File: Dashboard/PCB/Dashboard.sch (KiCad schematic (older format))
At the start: 91 parts, among them J1 Display, J2 Conn_01x26_Female, J3 LED, J7 PROGRAMMER, SW1 SW_SPST, U1 STM32F767ZIT6, U10 24LC01, U3 MP2359DJ-LF-Z, U4 AS4C1M16S-6TCN, U5 AT25SF128A-SHB-T, U6 MP2332H, U7 MCP2561-E-SN, U8 MCP2561-E-SN, U9 ESP-12S, Y1 Crystal_GND24

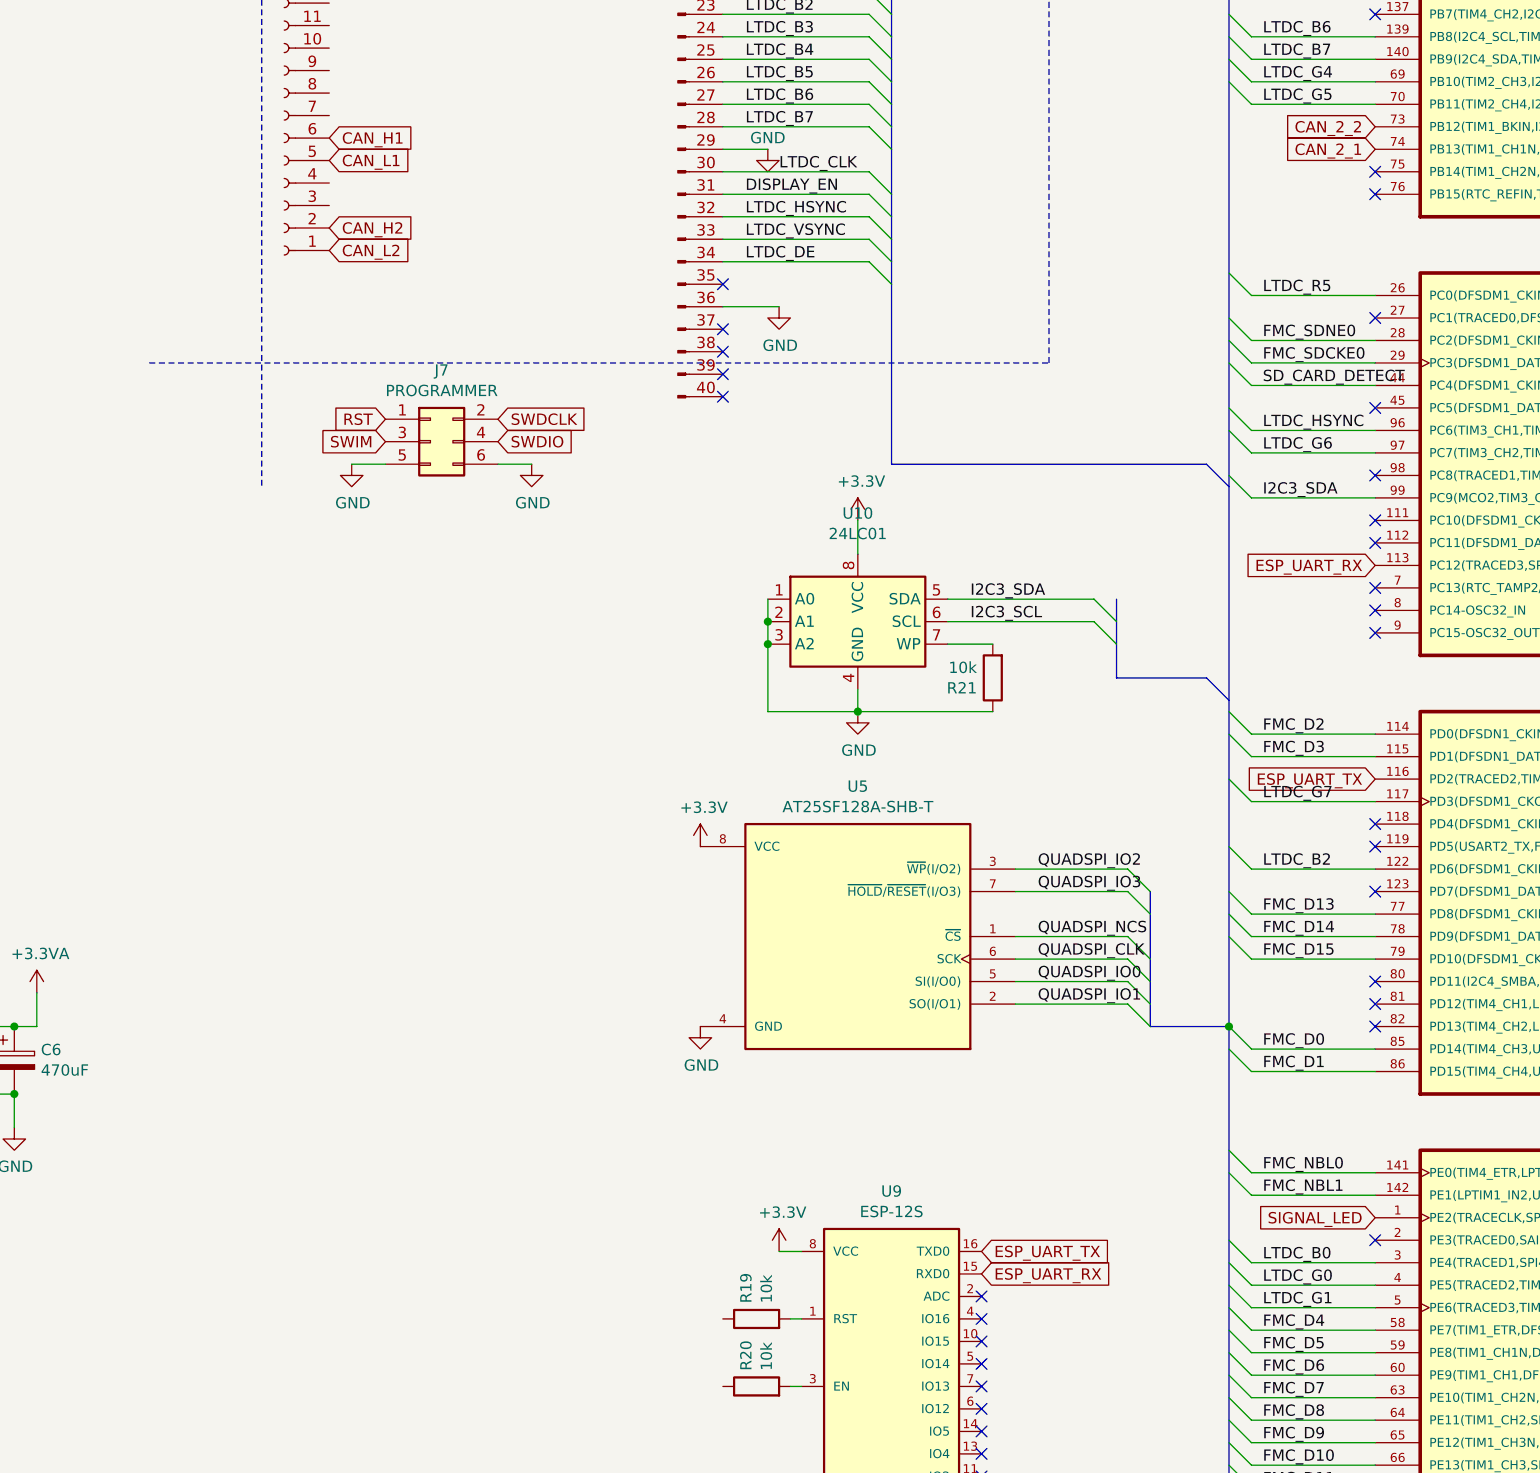
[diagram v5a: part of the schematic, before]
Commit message: Add usb C to board
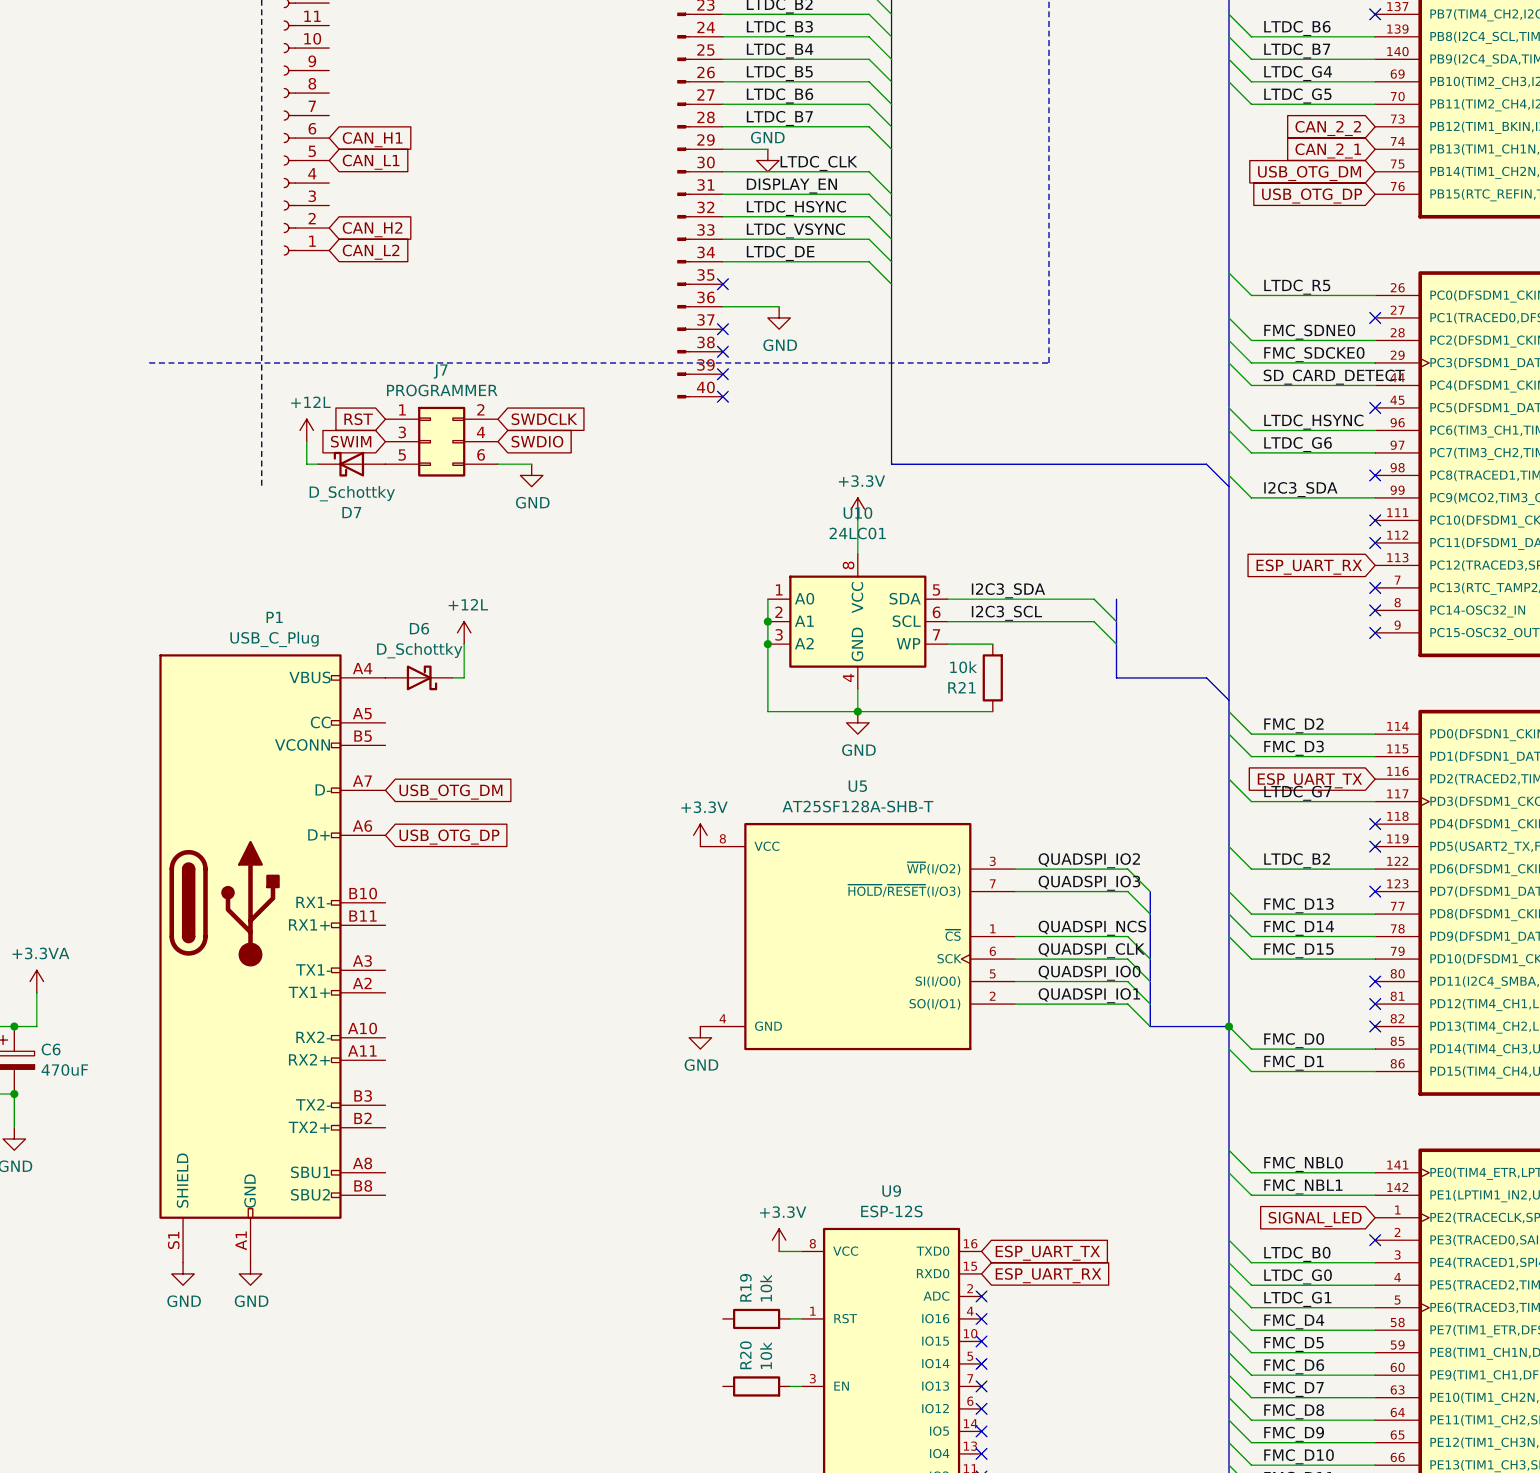
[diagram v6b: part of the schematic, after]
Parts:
- added D6, D7: D_Schottky, Diode_SMD:D_0805_2012Metric_Pad1.15x1.40mm_HandSolder, symbol Device:D_Schottky
- added P1: USB_C_Plug, Connector_USB:USB_C_Receptacle_Amphenol_12401548E4-2A, symbol Connector:USB_C_Plug
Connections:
- net +12L: now also D6.1 (K), D7.1 (K)
- net GND: now also P1.A1 (GND), P1.A12 (GND), P1.B1 (GND), P1.B12 (GND), P1.S1 (SHIELD); no longer J7.5 (Pin_5)
- net USB_OTG_DM: now reaches U1.75 (PB14(TIM1_CH2N,TIM8_CH2N,USART1_TX,SPI2_MISO,DFSDM1_DATIN2,USART3_RTS,UART4_RTS,TIM12_CH1,SDMMC2_D0,OTG_HS_DM))
- net USB_OTG_DM: now also P1.A7 (D-)
- net USB_OTG_DP: now reaches U1.76 (PB15(RTC_REFIN,TIM1_CH3N,TIM8_CH3N,USART1_RX,SPI2_MOSI/I2S2_SD,DFSDM1_CKIN2,UART4_CTS,TIM12_CH2,SDMMC2_D1,OTG_HS_DP))
- net USB_OTG_DP: now also P1.A6 (D+)
- new net: D6.2 (A), P1.A4 (VBUS), P1.A9 (VBUS), P1.B4 (VBUS), P1.B9 (VBUS)
- new net: D7.2 (A), J7.5 (Pin_5)
- no-connect marks 45 -> 43
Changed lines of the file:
@@
 CONNECTORS\n
-$Comp
-L power:GND #PWR052
-U 1 1 6256A616
-P 10650 5450
-F 0 "#PWR052" H 10650 5200 50  0001 C CNN
-F 1 "GND" H 10655 5277 50  0000 C CNN
-F 2 "" H 10650 5450 50  0001 C CNN
-F 3 "" H 10650 5450 50  0001 C CNN
-	1    10650 5450
-	1    0    0    -1
-$EndComp
 $Comp
 L power:GND #PWR059
@@
 	1    0    0    -1
 $EndComp
-Wire Wire Line
-	10650 5450 10800 5450
 Wire Wire Line
 	11300 5450 11450 5450
@@
 NoConn ~ 15200 7150
 NoConn ~ 15200 4800
-NoConn ~ 15200 4150
-NoConn ~ 15200 4250
 $Comp
 L Memory_EEPROM:24LC01 U10
@@
 	1    0    0    -1
 $EndComp
+Text GLabel 7000 9550 1    50   Input ~ 0
+SIGNAL_LED
+$Comp
+L Connector:USB_C_Plug P1
+U 1 1 62227F66
+P 10200 7400
+F 0 "P1" H 10307 8667 50  0000 C CNN
+F 1 "USB_C_Plug" H 10307 8576 50  0000 C CNN
+F 2 "Connector_USB:USB_C_Receptacle_Amphenol_12401548E4-2A" H 10350 7400 50  0001 C CNN
+F 3 "https://www.usb.org/sites/default/files/documents/usb_type-c.zip" H 10350 7400 50  0001 C CNN
+	1    10200 7400
+	1    0    0    -1
+$EndComp
+$Comp
+L power:GND #PWR0117
+U 1 1 6222BA60
+P 9900 9000
+F 0 "#PWR0117" H 9900 8750 50  0001 C CNN
+F 1 "GND" H 9905 8827 50  0000 C CNN
+F 2 "" H 9900 9000 50  0001 C CNN
+F 3 "" H 9900 9000 50  0001 C CNN
+	1    9900 9000
+	1    0    0    -1
+$EndComp
+$Comp
+L power:GND #PWR0118
+U 1 1 6222D943
+P 10200 9000
+F 0 "#PWR0118" H 10200 8750 50  0001 C CNN
+F 1 "GND" H 10205 8827 50  0000 C CNN
+F 2 "" H 10200 9000 50  0001 C CNN
+F 3 "" H 10200 9000 50  0001 C CNN
+	1    10200 9000
+	1    0    0    -1
+$EndComp
+Wire Wire Line
+	11150 6250 11150 6400
+Wire Wire Line
+	11150 6400 11100 6400
+$Comp
+L Device:D_Schottky D6
+U 1 1 6227A44E
+P 10950 6400
+F 0 "D6" H 10950 6183 50  0000 C CNN
+F 1 "D_Schottky" H 10950 6274 50  0000 C CNN
+F 2 "Diode_SMD:D_0805_2012Metric_Pad1.15x1.40mm_HandSolder" H 10950 6400 50  0001 C CNN
+F 3 "~" H 10950 6400 50  0001 C CNN
+	1    10950 6400
+	-1   0    0    1
+$EndComp
+$Comp
+L power:+12L #PWR0123
+U 1 1 6227CD2E
+P 11150 6250
+F 0 "#PWR0123" H 11150 6100 50  0001 C CNN
+F 1 "+12L" H 11165 6423 50  0000 C CNN
+F 2 "" H 11150 6250 50  0001 C CNN
+F 3 "" H 11150 6250 50  0001 C CNN
+	1    11150 6250
+	1    0    0    -1
+$EndComp
+Text GLabel 10800 7100 2    50   Input ~ 0
+USB_OTG_DP
+Text GLabel 10800 6900 2    50   Input ~ 0
+USB_OTG_DM
+Text GLabel 15200 4150 0    50   Input ~ 0
+USB_OTG_DM
+Text GLabel 15200 4250 0    50   Input ~ 0
+USB_OTG_DP
+Wire Wire Line
+	10450 5450 10500 5450
+$Comp
+L Device:D_Schottky D7
+U 1 1 623639C9
+P 10650 5450
+F 0 "D7" H 10650 5233 50  0000 C CNN
+F 1 "D_Schottky" H 10650 5324 50  0000 C CNN
+F 2 "Diode_SMD:D_0805_2012Metric_Pad1.15x1.40mm_HandSolder" H 10650 5450 50  0001 C CNN
+F 3 "~" H 10650 5450 50  0001 C CNN
+	1    10650 5450
+	1    0    0    -1
+$EndComp
+$Comp
+L power:+12L #PWR0127
+U 1 1 623639CF
+P 10450 5350
+F 0 "#PWR0127" H 10450 5200 50  0001 C CNN
+F 1 "+12L" H 10465 5523 50  0000 C CNN
+F 2 "" H 10450 5350 50  0001 C CNN
+F 3 "" H 10450 5350 50  0001 C CNN
+	1    10450 5350
+	1    0    0    -1
+$EndComp
+Wire Wire Line
+	10450 5450 10450 5350
 Wire Bus Line
 	14050 6050 14050 6400
@@
 Wire Bus Line
 	14550 7950 14550 14000
-Text GLabel 7000 9550 1    50   Input ~ 0
-SIGNAL_LED
 $EndSCHEMATC

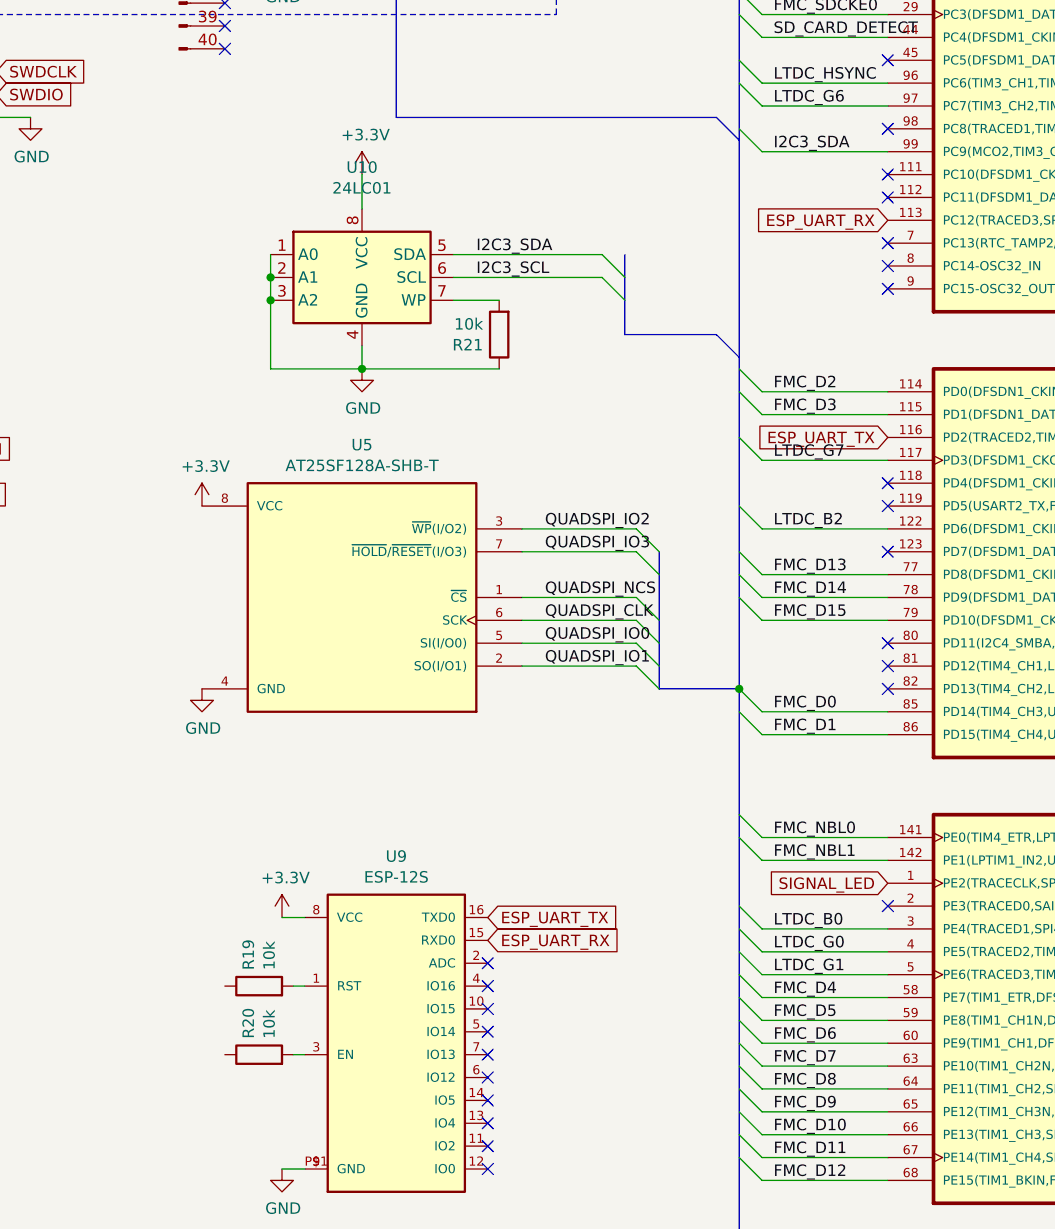
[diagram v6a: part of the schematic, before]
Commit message: Add reset and pd pin to esp
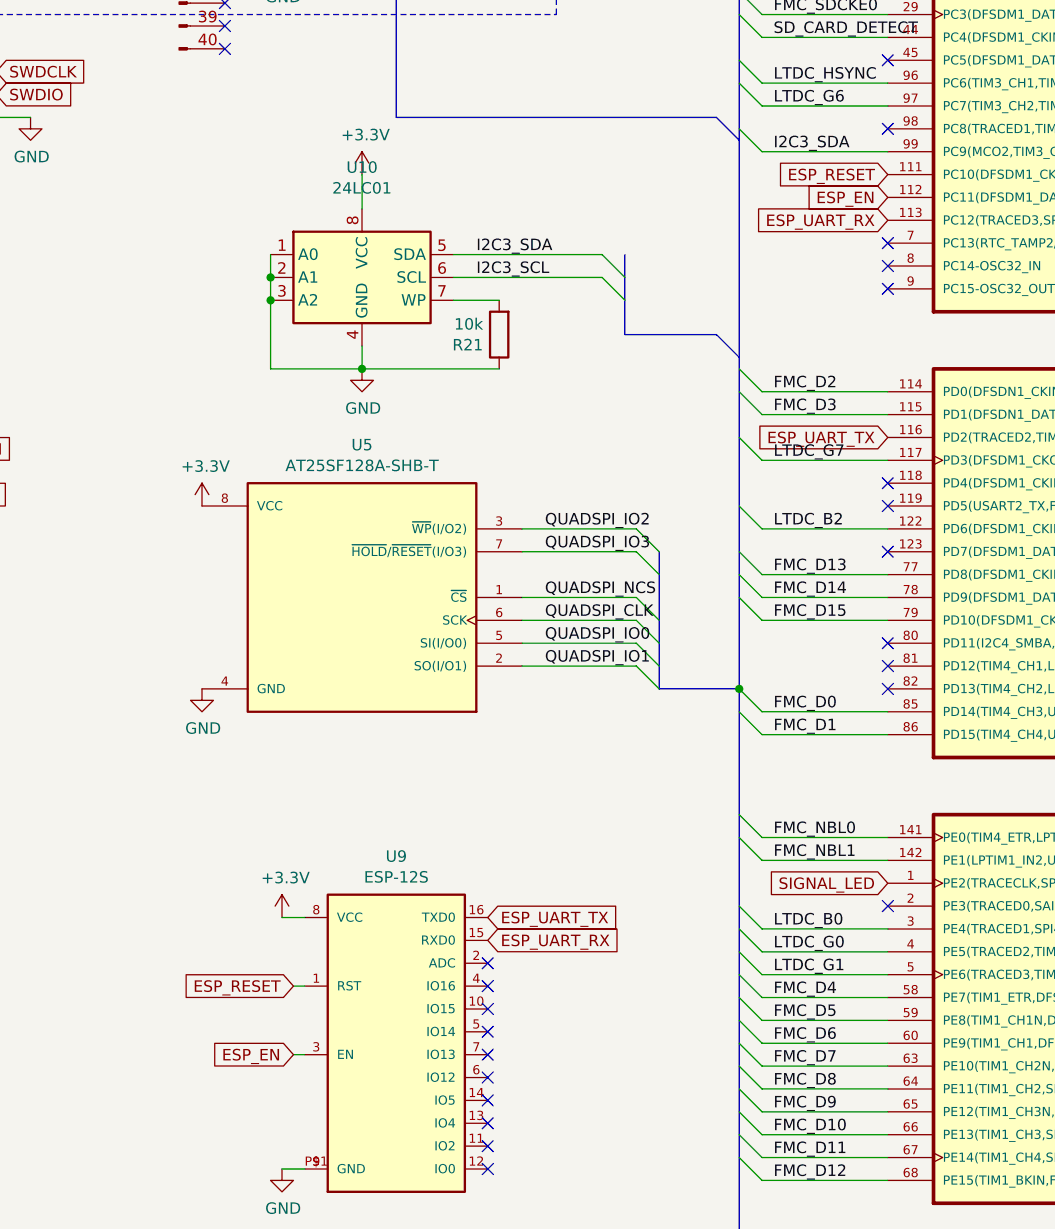
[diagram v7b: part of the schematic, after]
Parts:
- removed R19, R20: 10k, Resistor_SMD:R_0805_2012Metric, symbol Device:R
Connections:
- net ESP_RESET: now reaches U1.111 (PC10(DFSDM1_CKIN5,SPI3_SCK/I2S3_CK,USART3_TX,UART4_TX,QUADSPI_BK1_IO1,SDMMC1_D2,DCMI_D8,LCD_R2))
- net ESP_RESET: now also U9.1 (RST)
- net ESP_EN: now reaches U1.112 (PC11(DFSDM1_DATIN5,SPI3_MISO,USART3_RX,UART4_RX,QUADSPI_BK2_NCS,SDMMC1_D3,DCMI_D4))
- net ESP_EN: now also U9.3 (EN)
- no-connect marks 43 -> 41
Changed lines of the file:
@@
 $Comp
 L STM32F767ZIT6:STM32F767ZIT6 U1
-U 4 1 6179CCD7
-P 18600 5400
-F 0 "U1" H 18494 6370 50  0000 C CNN
-F 1 "STM32F767ZIT6" H 18494 6279 50  0000 C CNN
-F 2 "STM32F767ZIT6:QFP50P2200X2200X160-144N" H 18600 5400 50  0001 L BNN
-F 3 "" H 18600 5400 50  0001 L BNN
-F 4 "6" H 18600 5400 50  0001 L BNN "PARTREV"
-F 5 "STMicroelectronics" H 18600 5400 50  0001 L BNN "MF"
-F 6 "LQFP-144 STMicroelectronics" H 18600 5400 50  0001 L BNN "PACKAGE"
-F 7 "IPC-7351B" H 18600 5400 50  0001 L BNN "STANDARD"
-F 8 "IC MCU 32BIT 2MB FLASH 144LQFP" H 18600 5400 50  0001 L BNN "DESCRIPTION"
-F 9 "STM32F767ZIT6" H 18600 5400 50  0001 L BNN "MP"
-F 10 "14.84 USD" H 18600 5400 50  0001 L BNN "PRICE"
-F 11 "Good" H 18600 5400 50  0001 L BNN "AVAILABILITY"
-	4    18600 5400
-	1    0    0    -1
-$EndComp
-$Comp
-L STM32F767ZIT6:STM32F767ZIT6 U1
 U 8 1 617B5C05
 P 18100 13200
@@
 NoConn ~ 15200 5200
 NoConn ~ 15200 5500
-NoConn ~ 15200 5700
-NoConn ~ 15200 5800
 NoConn ~ 15200 6000
 NoConn ~ 15200 6100
@@
 Text Label 14700 3650 0    50   ~ 0
 LTDC_B7
-$Comp
-L Device:R R19
-U 1 1 62B4D0C1
-P 12450 9250
-F 0 "R19" H 12520 9296 50  0000 L CNN
-F 1 "10k" H 12520 9205 50  0000 L CNN
-F 2 "Resistor_SMD:R_0805_2012Metric" V 12380 9250 50  0001 C CNN
-F 3 "~" H 12450 9250 50  0001 C CNN
-	1    12450 9250
-	0    -1   -1   0
-$EndComp
-$Comp
-L Device:R R20
-U 1 1 62B93232
-P 12450 9550
-F 0 "R20" H 12520 9596 50  0000 L CNN
-F 1 "10k" H 12520 9505 50  0000 L CNN
-F 2 "Resistor_SMD:R_0805_2012Metric" V 12380 9550 50  0001 C CNN
-F 3 "~" H 12450 9550 50  0001 C CNN
-	1    12450 9550
-	0    -1   -1   0
-$EndComp
 Wire Wire Line
 	12650 9250 12600 9250
@@
 Wire Wire Line
 	10450 5450 10450 5350
+$Comp
+L STM32F767ZIT6:STM32F767ZIT6 U1
+U 4 1 6179CCD7
+P 18600 5400
+F 0 "U1" H 18494 6370 50  0000 C CNN
+F 1 "STM32F767ZIT6" H 18494 6279 50  0000 C CNN
+F 2 "STM32F767ZIT6:QFP50P2200X2200X160-144N" H 18600 5400 50  0001 L BNN
+F 3 "" H 18600 5400 50  0001 L BNN
+F 4 "6" H 18600 5400 50  0001 L BNN "PARTREV"
+F 5 "STMicroelectronics" H 18600 5400 50  0001 L BNN "MF"
+F 6 "LQFP-144 STMicroelectronics" H 18600 5400 50  0001 L BNN "PACKAGE"
+F 7 "IPC-7351B" H 18600 5400 50  0001 L BNN "STANDARD"
+F 8 "IC MCU 32BIT 2MB FLASH 144LQFP" H 18600 5400 50  0001 L BNN "DESCRIPTION"
+F 9 "STM32F767ZIT6" H 18600 5400 50  0001 L BNN "MP"
+F 10 "14.84 USD" H 18600 5400 50  0001 L BNN "PRICE"
+F 11 "Good" H 18600 5400 50  0001 L BNN "AVAILABILITY"
+	4    18600 5400
+	1    0    0    -1
+$EndComp
+Text GLabel 15200 5800 0    50   Input ~ 0
+ESP_EN
+Text GLabel 15200 5700 0    50   Input ~ 0
+ESP_RESET
 Wire Bus Line
 	14050 6050 14050 6400
@@
 Wire Bus Line
 	14550 7950 14550 14000
+Text GLabel 12600 9250 0    50   Input ~ 0
+ESP_RESET
+Text GLabel 12600 9550 0    50   Input ~ 0
+ESP_EN
 $EndSCHEMATC

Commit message: Switch footprints of converter
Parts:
- U3: footprint Package_SO:SOIC-8-1EP_3.9x4.9mm_P1.27mm_EP2.29x3mm -> SOT-583:SOTFL50P160X60-8N
- U6: footprint SOT-583:SOTFL50P160X60-8N -> Package_SO:SOIC-8-1EP_3.9x4.9mm_P1.27mm_EP2.29x3mm
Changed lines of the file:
@@
 F 0 "U3" H 3450 7815 50  0000 C CNN
 F 1 "MP2359DJ-LF-Z" H 3450 7724 50  0000 C CNN
-F 2 "Package_SO:SOIC-8-1EP_3.9x4.9mm_P1.27mm_EP2.29x3mm" H 3450 7700 50  0001 C CNN
+F 2 "SOT-583:SOTFL50P160X60-8N" H 3450 7700 50  0001 C CNN
 F 3 "" H 3450 7700 50  0001 C CNN
 	1    3450 7700
@@
 F 0 "U6" H 3450 9225 50  0000 C CNN
 F 1 "MP2332H" H 3450 9134 50  0000 C CNN
-F 2 "SOT-583:SOTFL50P160X60-8N" H 3450 9200 50  0001 C CNN
+F 2 "Package_SO:SOIC-8-1EP_3.9x4.9mm_P1.27mm_EP2.29x3mm" H 3450 9200 50  0001 C CNN
 F 3 "" H 3450 9200 50  0001 C CNN
 	1    3450 9200
